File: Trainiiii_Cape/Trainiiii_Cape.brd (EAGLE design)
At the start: 160 x 100 mm, 24 parts, among them J1 455-1750-1-ND, J2 455-1750-1-ND, Q1 220mA/50V/3.5Ω, Q2 220mA/50V/3.5Ω

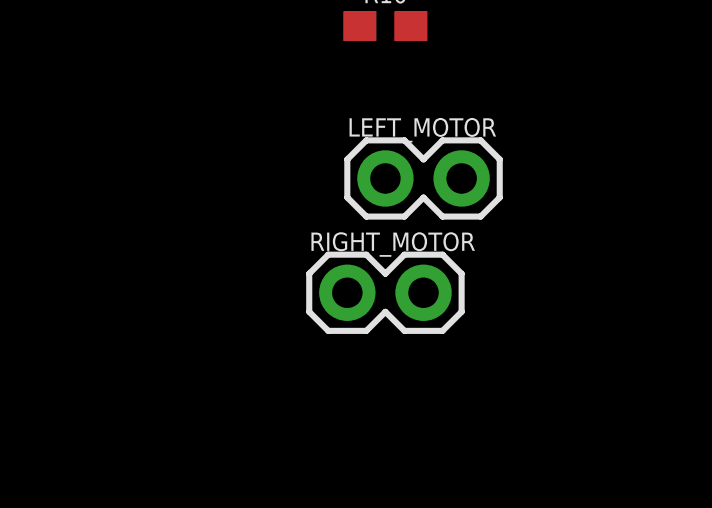
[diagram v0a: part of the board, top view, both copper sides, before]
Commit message: Organization and pin changes.
Moved ultrasonic lines to pins that don't interfere with BBB boot sequence. Began organizing things into sheets!
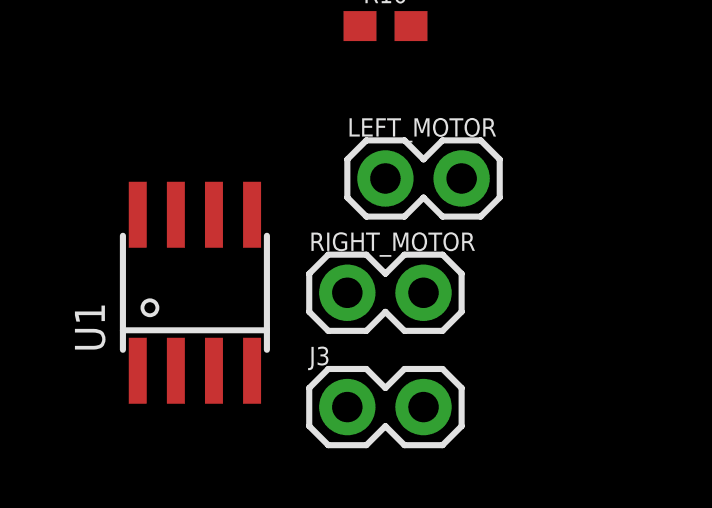
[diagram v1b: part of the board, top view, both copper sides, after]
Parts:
- added J3: (no value), SparkFun-Connectors:1X02
- added U1: AP1509-50, RoboJackets-PowerICs:SOIC-8
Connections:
- new net POWER_BUTTON: B1.P9.9, J3.2
- net 5V: now also B1.P9.5, B1.P9.6; no longer B1.P9.7, B1.P9.8
- net GND: now also J3.1, U1.4, U1.5, U1.6, U1.7, U1.8
- net US_ECHO_3V3: now also B1.P8.17; no longer B1.P8.46
- net US_TRIGGER_3V3: now also B1.P8.15; no longer B1.P8.45
- net V_BATT: now also U1.1
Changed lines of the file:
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@@
 <attribute name="VALUE" x="-100.33" y="-51.562" size="0.6096" layer="27" font="vector" ratio="20"/>
+</element>
+<element name="J3" library="SparkFun-Connectors" package="1X02" value="" x="-99.06" y="-53.34" smashed="yes">
+<attribute name="NAME" x="-100.33" y="-51.943" size="0.6096" layer="25" font="vector" ratio="20"/>
+<attribute name="VALUE" x="-100.33" y="-55.372" size="0.6096" layer="27" font="vector" ratio="20"/>
+</element>
+<element name="U1" library="RoboJackets-PowerICs" package="SOIC-8" value="AP1509-50" x="-104.14" y="-49.53" smashed="yes">
+<attribute name="NAME" x="-107.14" y="-51.53" size="1" layer="25" rot="R90"/>
 </element>
 </elements>
@@
 <contactref element="R7" pad="2"/>
 <contactref element="R8" pad="2"/>
+<contactref element="J3" pad="1"/>
+<contactref element="U1" pad="5"/>
+<contactref element="U1" pad="6"/>
+<contactref element="U1" pad="7"/>
+<contactref element="U1" pad="8"/>
+<contactref element="U1" pad="4"/>
+<wire x1="-102.235" y1="-52.13" x2="-99.06" y2="-53.34" width="0" layer="19" extent="1-1"/>
+<wire x1="-102.235" y1="-46.93" x2="-102.235" y2="-52.13" width="0" layer="19" extent="1-1"/>
+<wire x1="-103.505" y1="-46.93" x2="-102.235" y2="-46.93" width="0" layer="19" extent="1-1"/>
+<wire x1="-104.775" y1="-46.93" x2="-103.505" y2="-46.93" width="0" layer="19" extent="1-1"/>
+<wire x1="-106.045" y1="-46.93" x2="-104.775" y2="-46.93" width="0" layer="19" extent="1-1"/>
+<wire x1="-96.94" y1="-33.02" x2="-102.235" y2="-46.93" width="0" layer="19" extent="1-1"/>
 <wire x1="-96.94" y1="-29.21" x2="-96.94" y2="-33.02" width="0" layer="19" extent="1-1"/>
 <wire x1="-97.79" y1="-24.13" x2="-96.94" y2="-29.21" width="0" layer="19" extent="1-1"/>
@@
 <wire x1="-97.79" y1="-6.35" x2="-97.79" y2="-19.05" width="0" layer="19" extent="1-1"/>
 <wire x1="-97.79" y1="-2.54" x2="-97.79" y2="-6.35" width="0" layer="19" extent="1-1"/>
-<wire x1="20.32" y1="1.905" x2="-97.79" y2="-2.54" width="0" layer="19" extent="1-1"/>
-<wire x1="20.32" y1="4.445" x2="20.32" y2="1.905" width="0" layer="19" extent="1-1"/>
-<wire x1="60.96" y1="4.445" x2="20.32" y2="4.445" width="0" layer="19" extent="1-1"/>
-<wire x1="73.66" y1="4.445" x2="60.96" y2="4.445" width="0" layer="19" extent="1-1"/>
-<wire x1="73.66" y1="1.905" x2="73.66" y2="4.445" width="0" layer="19" extent="1-1"/>
-<wire x1="76.2" y1="1.905" x2="73.66" y2="1.905" width="0" layer="19" extent="1-1"/>
-<wire x1="76.2" y1="4.445" x2="73.66" y2="4.445" width="0" layer="19" extent="1-1"/>
-<wire x1="20.32" y1="50.165" x2="20.32" y2="4.445" width="0" layer="19" extent="1-1"/>
-<wire x1="20.32" y1="52.705" x2="20.32" y2="50.165" width="0" layer="19" extent="1-1"/>
-<wire x1="-71.81" y1="60.96" x2="20.32" y2="52.705" width="0" layer="19" extent="1-1"/>
+<wire x1="-71.81" y1="60.96" x2="-97.79" y2="-2.54" width="0" layer="19" extent="1-1"/>
 <wire x1="-68" y1="60.96" x2="-71.81" y2="60.96" width="0" layer="19" extent="1-1"/>
 <wire x1="-50.8" y1="72.39" x2="-68" y2="60.96" width="0" layer="19" extent="1-1"/>
@@
 <wire x1="-15.505" y1="61.114" x2="-16.155" y2="61.114" width="0" layer="19" extent="1-1"/>
 <wire x1="-17.455" y1="68.426" x2="-16.155" y2="61.114" width="0" layer="19" extent="1-1"/>
+<wire x1="20.32" y1="52.705" x2="-15.505" y2="61.114" width="0" layer="19" extent="1-1"/>
+<wire x1="20.32" y1="50.165" x2="20.32" y2="52.705" width="0" layer="19" extent="1-1"/>
+<wire x1="20.32" y1="4.445" x2="20.32" y2="50.165" width="0" layer="19" extent="1-1"/>
+<wire x1="20.32" y1="1.905" x2="20.32" y2="4.445" width="0" layer="19" extent="1-1"/>
+<wire x1="60.96" y1="4.445" x2="20.32" y2="4.445" width="0" layer="19" extent="1-1"/>
+<wire x1="73.66" y1="4.445" x2="60.96" y2="4.445" width="0" layer="19" extent="1-1"/>
+<wire x1="76.2" y1="4.445" x2="73.66" y2="4.445" width="0" layer="19" extent="1-1"/>
+<wire x1="76.2" y1="1.905" x2="76.2" y2="4.445" width="0" layer="19" extent="1-1"/>
+<wire x1="73.66" y1="1.905" x2="73.66" y2="4.445" width="0" layer="19" extent="1-1"/>
 </signal>
 <signal name="3.3V">
@@
 <contactref element="C1" pad="1"/>
 <contactref element="C3" pad="1"/>
+<contactref element="U1" pad="1"/>
+<wire x1="-72.97" y1="60.96" x2="-106.045" y2="-52.13" width="0" layer="19" extent="1-1"/>
+<wire x1="-69.16" y1="60.96" x2="-72.97" y2="60.96" width="0" layer="19" extent="1-1"/>
+<wire x1="-21.355" y1="68.426" x2="-69.16" y2="60.96" width="0" layer="19" extent="1-1"/>
+<wire x1="-14.855" y1="68.426" x2="-21.355" y2="68.426" width="0" layer="19" extent="1-1"/>
 <wire x1="-14.205" y1="68.426" x2="-14.855" y2="68.426" width="0" layer="19" extent="1-1"/>
-<wire x1="-21.355" y1="68.426" x2="-14.855" y2="68.426" width="0" layer="19" extent="1-1"/>
-<wire x1="-69.16" y1="60.96" x2="-21.355" y2="68.426" width="0" layer="19" extent="1-1"/>
-<wire x1="-72.97" y1="60.96" x2="-69.16" y2="60.96" width="0" layer="19" extent="1-1"/>
 </signal>
 <signal name="MOTOR_LEFT_PWM">
@@
 </signal>
 <signal name="5V">
-<contactref element="B1" pad="P9.7"/>
-<contactref element="B1" pad="P9.8"/>
 <contactref element="R2" pad="1"/>
 <contactref element="R4" pad="1"/>
@@
 <contactref element="J1" pad="2"/>
 <contactref element="J2" pad="2"/>
+<contactref element="B1" pad="P9.5"/>
+<contactref element="B1" pad="P9.6"/>
 <wire x1="-95.25" y1="-19.05" x2="-95.25" y2="-24.13" width="0" layer="19" extent="1-1"/>
 <wire x1="-92.71" y1="-6.35" x2="-95.25" y2="-19.05" width="0" layer="19" extent="1-1"/>
@@
 <wire x1="-92.71" y1="-2.54" x2="-92.71" y2="-6.35" width="0" layer="19" extent="1-1"/>
 <wire x1="-90.17" y1="-2.54" x2="-92.71" y2="-2.54" width="0" layer="19" extent="1-1"/>
-<wire x1="27.94" y1="1.905" x2="-90.17" y2="-2.54" width="0" layer="19" extent="1-1"/>
-<wire x1="27.94" y1="4.445" x2="27.94" y2="1.905" width="0" layer="19" extent="1-1"/>
-<wire x1="-64.35" y1="77.47" x2="27.94" y2="4.445" width="0" layer="19" extent="1-1"/>
+<wire x1="-64.35" y1="77.47" x2="-90.17" y2="-2.54" width="0" layer="19" extent="1-1"/>
 <wire x1="-64.35" y1="80.01" x2="-64.35" y2="77.47" width="0" layer="19" extent="1-1"/>
 <wire x1="-50.8" y1="80.01" x2="-64.35" y2="80.01" width="0" layer="19" extent="1-1"/>
+<wire x1="25.4" y1="4.445" x2="-50.8" y2="80.01" width="0" layer="19" extent="1-1"/>
+<wire x1="25.4" y1="1.905" x2="25.4" y2="4.445" width="0" layer="19" extent="1-1"/>
 </signal>
 <signal name="US_ECHO_3V3">
 <contactref element="Q1" pad="2"/>
 <contactref element="R1" pad="2"/>
-<contactref element="B1" pad="P8.46"/>
+<contactref element="B1" pad="P8.17"/>
+<wire x1="-38.37" y1="74.61" x2="40.64" y2="50.165" width="0" layer="19" extent="1-1"/>
 <wire x1="-52.49" y1="60.96" x2="-38.37" y2="74.61" width="0" layer="19" extent="1-1"/>
-<wire x1="76.2" y1="52.705" x2="-38.37" y2="74.61" width="0" layer="19" extent="1-1"/>
 </signal>
 <signal name="US_TRIGGER_5V">
@@
 <contactref element="Q2" pad="2"/>
 <contactref element="R3" pad="2"/>
-<contactref element="B1" pad="P8.45"/>
+<contactref element="B1" pad="P8.15"/>
+<wire x1="-38.37" y1="79.69" x2="38.1" y2="50.165" width="0" layer="19" extent="1-1"/>
 <wire x1="-60.11" y1="60.96" x2="-38.37" y2="79.69" width="0" layer="19" extent="1-1"/>
-<wire x1="76.2" y1="50.165" x2="-38.37" y2="79.69" width="0" layer="19" extent="1-1"/>
 </signal>
 <signal name="ENCODER_LEFT_SIGNAL">
@@
 <wire x1="-14.205" y1="61.114" x2="-14.855" y2="61.114" width="0" layer="19" extent="1-1"/>
 </signal>
+<signal name="POWER_BUTTON">
+<contactref element="J3" pad="2"/>
+<contactref element="B1" pad="P9.9"/>
+<wire x1="30.48" y1="1.905" x2="-96.52" y2="-53.34" width="0" layer="19" extent="1-1"/>
+</signal>
 </signals>
